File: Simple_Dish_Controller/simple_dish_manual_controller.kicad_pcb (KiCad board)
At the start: 4 copper layers, 46 parts, among them J1 Screw_Terminal_01x02, J2 Conn_01x02_Pin, J3 Screw Terminal To Chassis, J4 Conn_01x03_Pin, J5 Elevation DE-15, J6 Conn_01x03_Pin, J7 Azimuth DE-15, Q1 MMBT2222A, Q2 MMBT2222A, Q3 MMBT2222A, Q4 MMBT2222A, U1 AMS1117-5.0, U2 74LS32, U3 74LS08, U4 NE555D, U5 NE555D

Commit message: Updates
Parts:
- added REF**: Raspberry_Pi_HAT_Side_DE15_Outline, DishFootprints:Raspberry_Pi_HAT_Side_DE15_Outline, F.Cu at (170.5, 47.4)
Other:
- board outline added: 65 x 75 mm
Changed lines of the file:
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@@
 		)
 		(embedded_fonts no)
-		(model "${KICAD_USER_PARTS}/supplier_parts/3d_models/L77HDE15SD1CH4FVGA.step"
+		(model "${DISH_3RD_PARTY}/3d_models/L77HDE15SD1CH4FVGA.step"
 			(offset
 				(xyz 0 -11 5.5)
@@
 		)
 	)
+	(footprint "DishFootprints:Raspberry_Pi_HAT_Side_DE15_Outline"
+		(layer "F.Cu")
+		(at 170.5 47.4)
+		(descr "Raspberry Pi HAT standard outline with mounting holes")
+		(tags "Raspberry Pi HAT")
+		(property "Reference" "REF**"
+			(at 0 0 0)
+			(layer "F.SilkS")
+			(hide yes)
+			(effects
+				(font
+					(size 1 1)
+					(thickness 0.15)
+				)
+			)
+		)
+		(property "Value" "Raspberry_Pi_HAT_Side_DE15_Outline"
+			(at 0 -5 0)
+			(layer "F.Fab")
+			(effects
+				(font
+					(size 1 1)
+					(thickness 0.15)
+				)
+			)
+		)
+		(property "Datasheet" ""
+			(at 0 0 0)
+			(layer "F.Fab")
+			(hide yes)
+			(effects
+				(font
+					(size 1.27 1.27)
+					(thickness 0.15)
+				)
+			)
+		)
+		(property "Description" "Raspberry Pi HAT outline with holes"
+			(at 0 0 0)
+			(layer "F.Fab")
+			(hide yes)
+			(effects
+				(font
+					(size 1.27 1.27)
+					(thickness 0.15)
+				)
+			)
+		)
+		(property "Note" "From a ChatGPT discussion"
+			(at 0 0 0)
+			(layer "F.SilkS")
+			(effects
+				(font
+					(size 1 1)
+					(thickness 0.1)
+				)
+			)
+		)
+		(attr exclude_from_pos_files exclude_from_bom)
+		(fp_line
+			(start 0 0)
+			(end 65 0)
+			(stroke
+				(width 0.05)
+				(type solid)
+			)
+			(layer "Edge.Cuts")
+		)
+		(fp_line
+			(start 0 75)
+			(end 0 0)
+			(stroke
+				(width 0.05)
+				(type solid)
+			)
+			(layer "Edge.Cuts")
+		)
+		(fp_line
+			(start 65 0)
+			(end 65 75)
+			(stroke
+				(width 0.05)
+				(type solid)
+			)
+			(layer "Edge.Cuts")
+		)
+		(fp_line
+			(start 65 75)
+			(end 0 75)
+			(stroke
+				(width 0.05)
+				(type solid)
+			)
+			(layer "Edge.Cuts")
+		)
+		(pad "" np_thru_hole circle
+			(at 2.5 2.5)
+			(size 2.75 2.75)
+			(drill 2.75)
+			(layers "*.Mask")
+		)
+		(pad "" np_thru_hole circle
+			(at 2.5 53.5)
+			(size 2.75 2.75)
+			(drill 2.75)
+			(layers "*.Mask")
+		)
+		(pad "" np_thru_hole circle
+			(at 62.5 2.5)
+			(size 2.75 2.75)
+			(drill 2.75)
+			(layers "*.Mask")
+		)
+		(pad "" np_thru_hole circle
+			(at 62.5 53.5)
+			(size 2.75 2.75)
+			(drill 2.75)
+			(layers "*.Mask")
+		)
+		(embedded_fonts no)
+	)
 	(footprint "Resistor_SMD:R_1206_3216Metric"
 		(layer "F.Cu")
@@
 		)
 		(embedded_fonts no)
-		(model "${KICAD_USER_PARTS}/supplier_parts/3d_models/7690.step"
+		(model "${DISH_3RD_PARTY}/3d_models/7690.step"
 			(offset
 				(xyz -3 4 1.5)
@@
 		)
 		(embedded_fonts no)
-		(model "${KICAD_USER_PARTS}/supplier_parts/3d_models/L77HDE15SD1CH4FVGA.step"
+		(model "${DISH_3RD_PARTY}/3d_models/L77HDE15SD1CH4FVGA.step"
 			(offset
 				(xyz 0 -11 5.5)

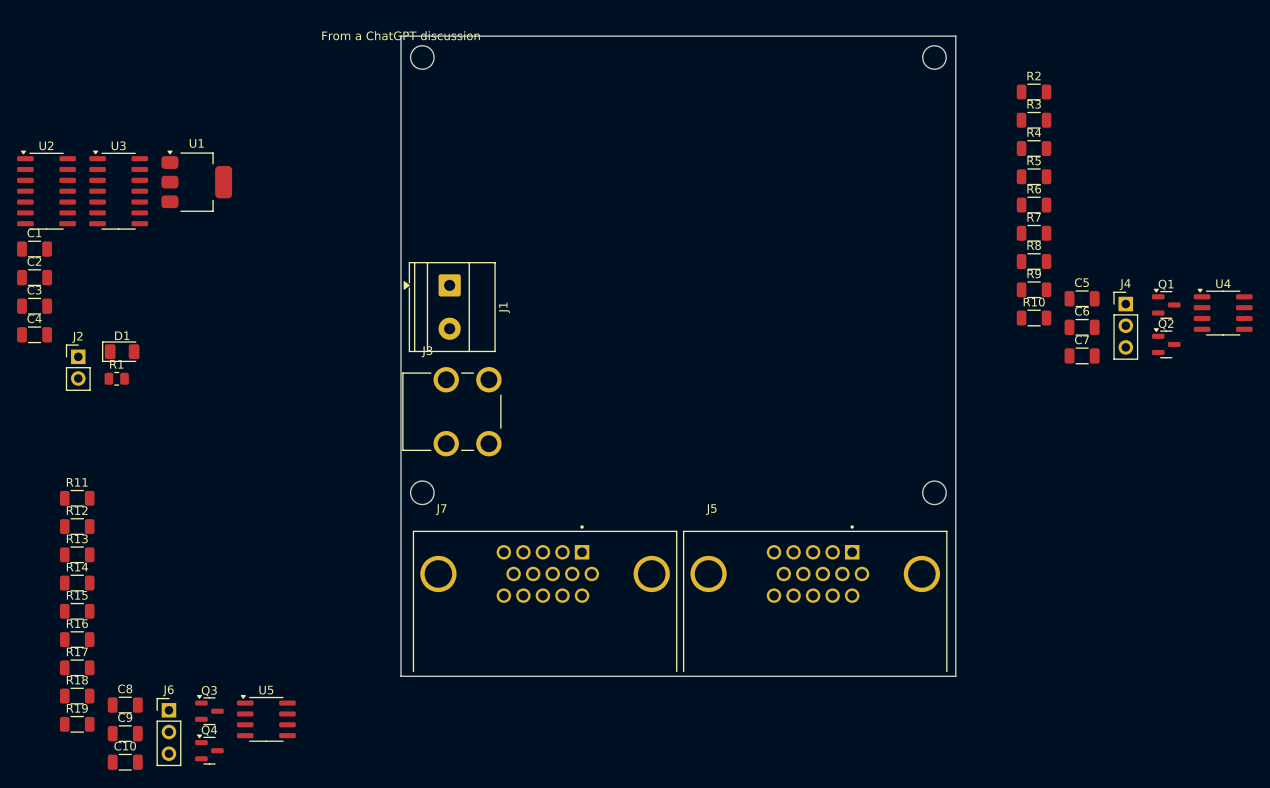
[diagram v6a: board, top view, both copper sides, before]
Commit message: PCB outline defined, origin and drill holes established, hole positioning completed. Beginning component placement.
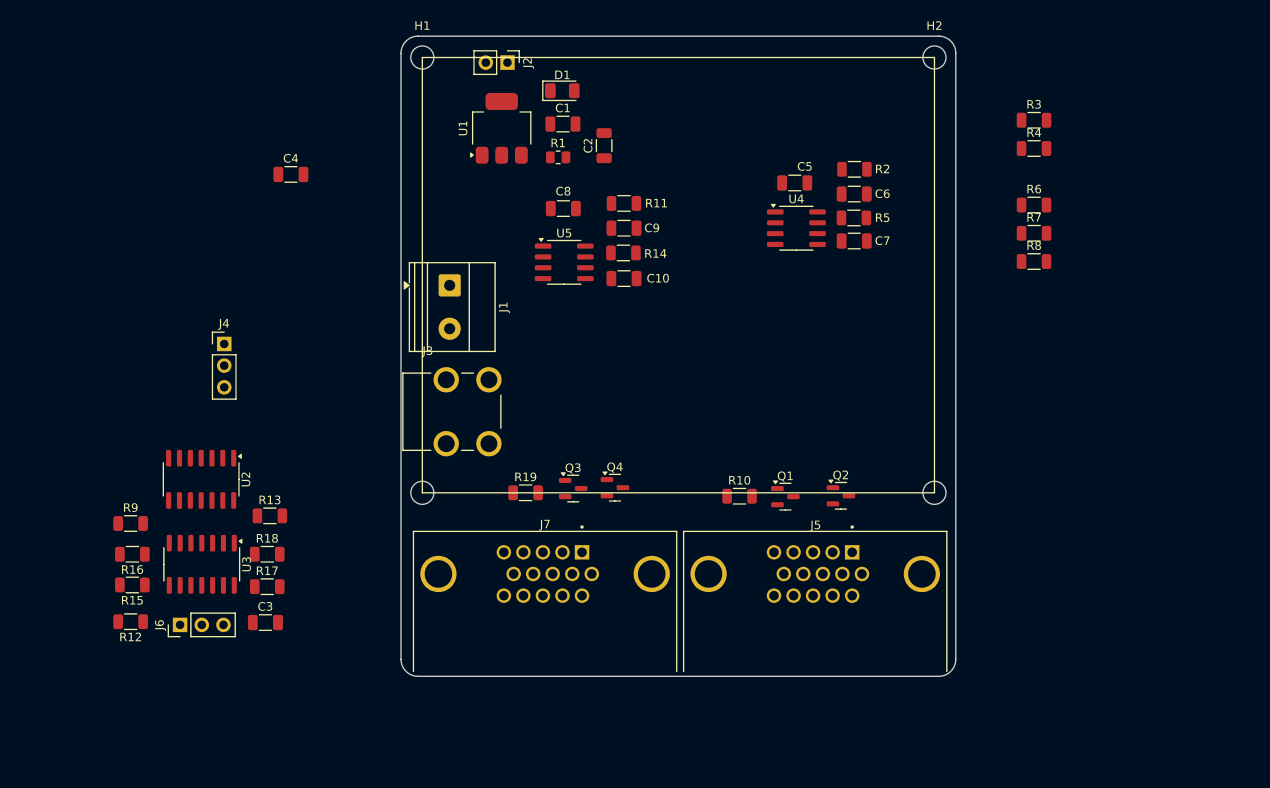
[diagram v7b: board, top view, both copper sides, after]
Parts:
- removed REF**: Raspberry_Pi_HAT_Side_DE15_Outline, DishFootprints:Raspberry_Pi_HAT_Side_DE15_Outline
- added H1: MountingHole, MountingHole:MountingHole_2.7mm_M2.5, F.Cu at (173.0, 49.9)
- added H2: MountingHole, MountingHole:MountingHole_2.7mm_M2.5, F.Cu at (233.0, 49.9)
- added H3: MountingHole, MountingHole:MountingHole_2.7mm_M2.5, F.Cu at (233.0, 100.9)
- added H4: MountingHole, MountingHole:MountingHole_2.7mm_M2.5, F.Cu at (173.0, 100.9)
- moved R9 109.3 mm to (138.8, 104.5)
- moved J4 105.7 mm to (149.8, 83.5)
- moved C9 83.2 mm to (196.6, 69.9)
- moved C10 81.4 mm to (196.6, 75.8)
- moved C8 77.6 mm to (189.5, 67.6), turned to 180 degrees
- moved R14 74.8 mm to (196.6, 72.8), turned to 180 degrees
- moved R11 72.8 mm to (196.6, 67.0), turned to 180 degrees
- moved C2 68.5 mm to (194.3, 60.2), turned to 90 degrees
- moved U5 63.9 mm to (189.6, 73.9)
- moved C1 63.6 mm to (189.5, 57.7)
- moved J2 61.0 mm to (183.0, 50.5), turned to -90 degrees
- moved D1 59.9 mm to (189.4, 53.8)
- moved R19 59.1 mm to (185.1, 100.9)
- moved R1 57.9 mm to (188.9, 61.6)
- moved Q4 56.6 mm to (195.6, 100.3)
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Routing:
- added copper zone on In1.Cu, net +5V
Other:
- outline, holes or cut-outs redrawn

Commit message: Component placement
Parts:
- moved R9 70.9 mm to (205.8, 81.4), turned to 90 degrees
- moved R12 70.4 mm to (190.0, 67.6)
- moved J6 70.1 mm to (195.1, 67.6)
- moved J4 69.2 mm to (217.1, 67.6), turned to 90 degrees
- moved R15 68.0 mm to (196.8, 75.9), turned to 90 degrees
- moved R17 66.9 mm to (205.2, 67.9)
- moved U2 66.8 mm to (212.0, 83.9), turned to 180 degrees
- moved C4 59.0 mm to (209.6, 91.6), turned to -90 degrees
- moved R16 58.8 mm to (193.1, 84.9), turned to 90 degrees
- moved U3 58.0 mm to (199.3, 83.9), turned to 180 degrees
- moved R4 52.9 mm to (201.8, 91.6), turned to -90 degrees
- moved C3 48.8 mm to (196.8, 91.7), turned to -90 degrees
- moved R13 44.8 mm to (193.1, 79.7), turned to 90 degrees
- moved R18 41.9 mm to (193.1, 90.8), turned to -90 degrees
- moved R6 38.8 mm to (214.6, 91.6), turned to -90 degrees
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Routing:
- added copper zone on In2.Cu, net +5V
- added copper zone on In1.Cu, net GND
- removed copper zone on In1.Cu, net +5V
